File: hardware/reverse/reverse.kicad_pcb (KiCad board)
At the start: 2 copper layers, 40 x 40 mm, 41 parts, among them J1 Conn_01x04, J2 Conn_01x03, T1 TestPoint_THTPad_3.0x3.0mm_Dr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, T51 TestPoint_THTPad_D2.0mm_Drill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, T52 TestPoint_THTPad_D2.0mm_Drill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, T53 TestPoint_THTPad_D2.0mm_Drill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, T54 TestPoint_THTPad_D2.0mm_Drill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, T55 TestPoint_THTPad_D2.0mm_Drill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, T56 TestPoint_THTPad_D2.0mm_Drill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, U1 WCH CH32V003F4U6

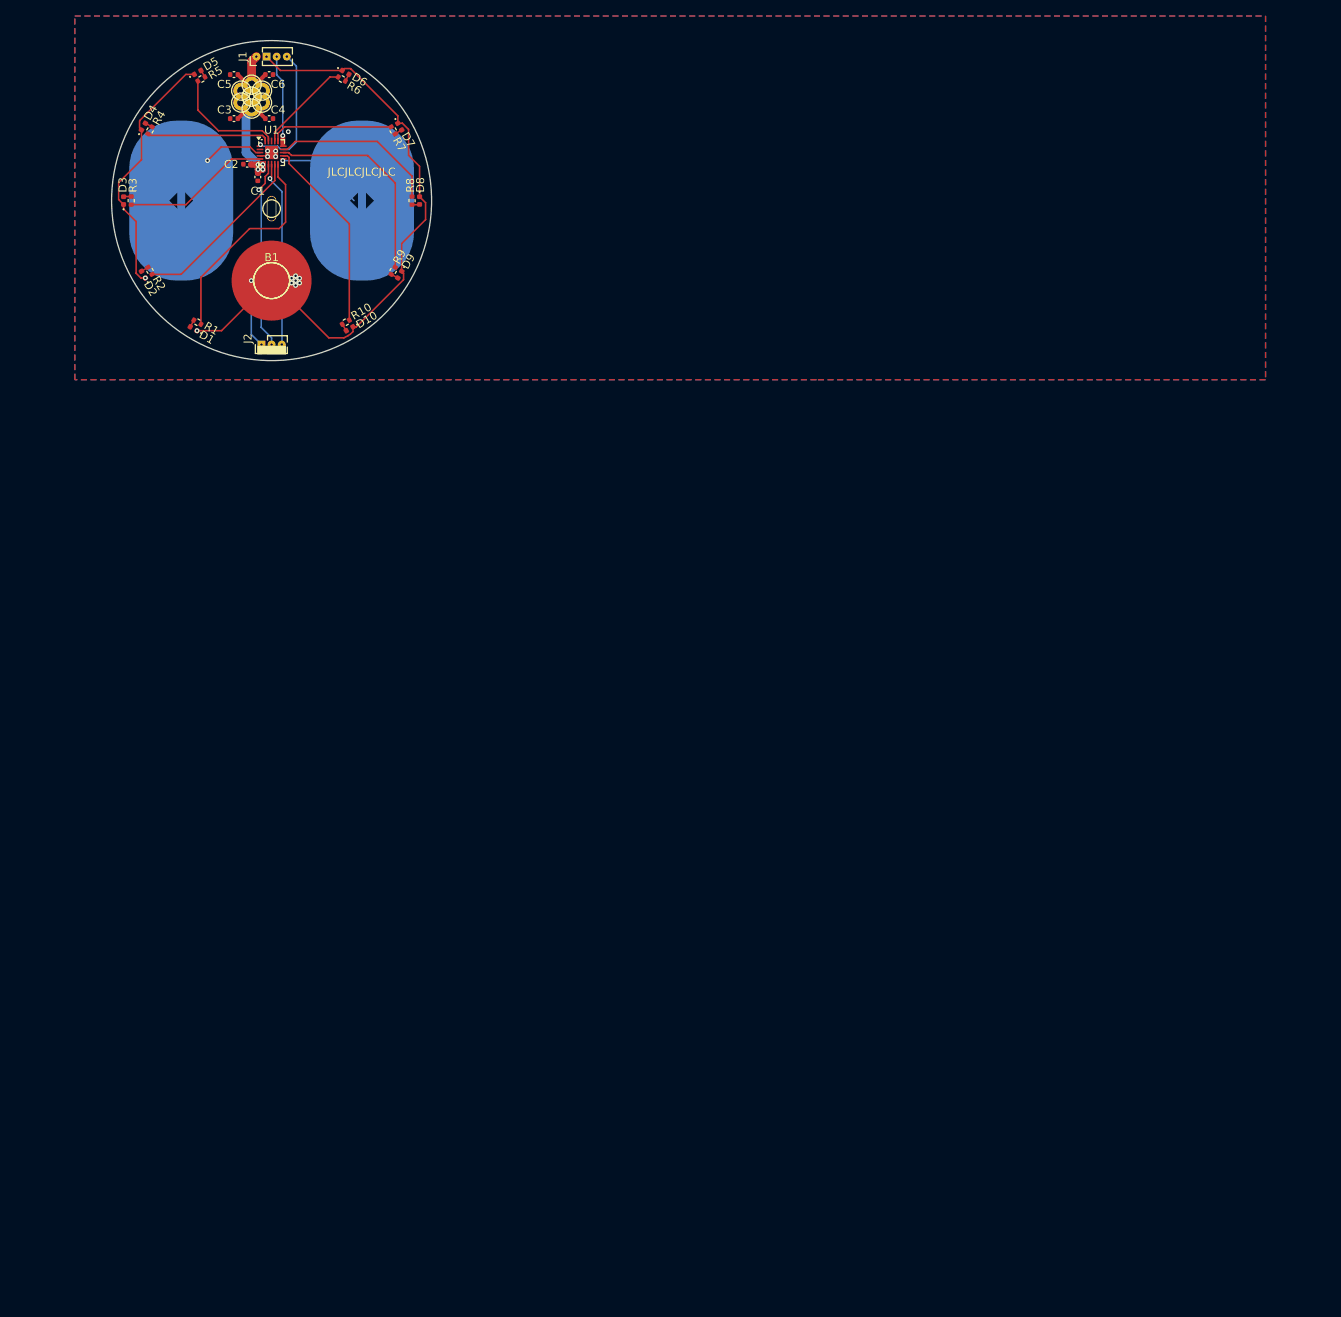
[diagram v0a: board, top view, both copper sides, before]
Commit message: separate boards and generate fab files
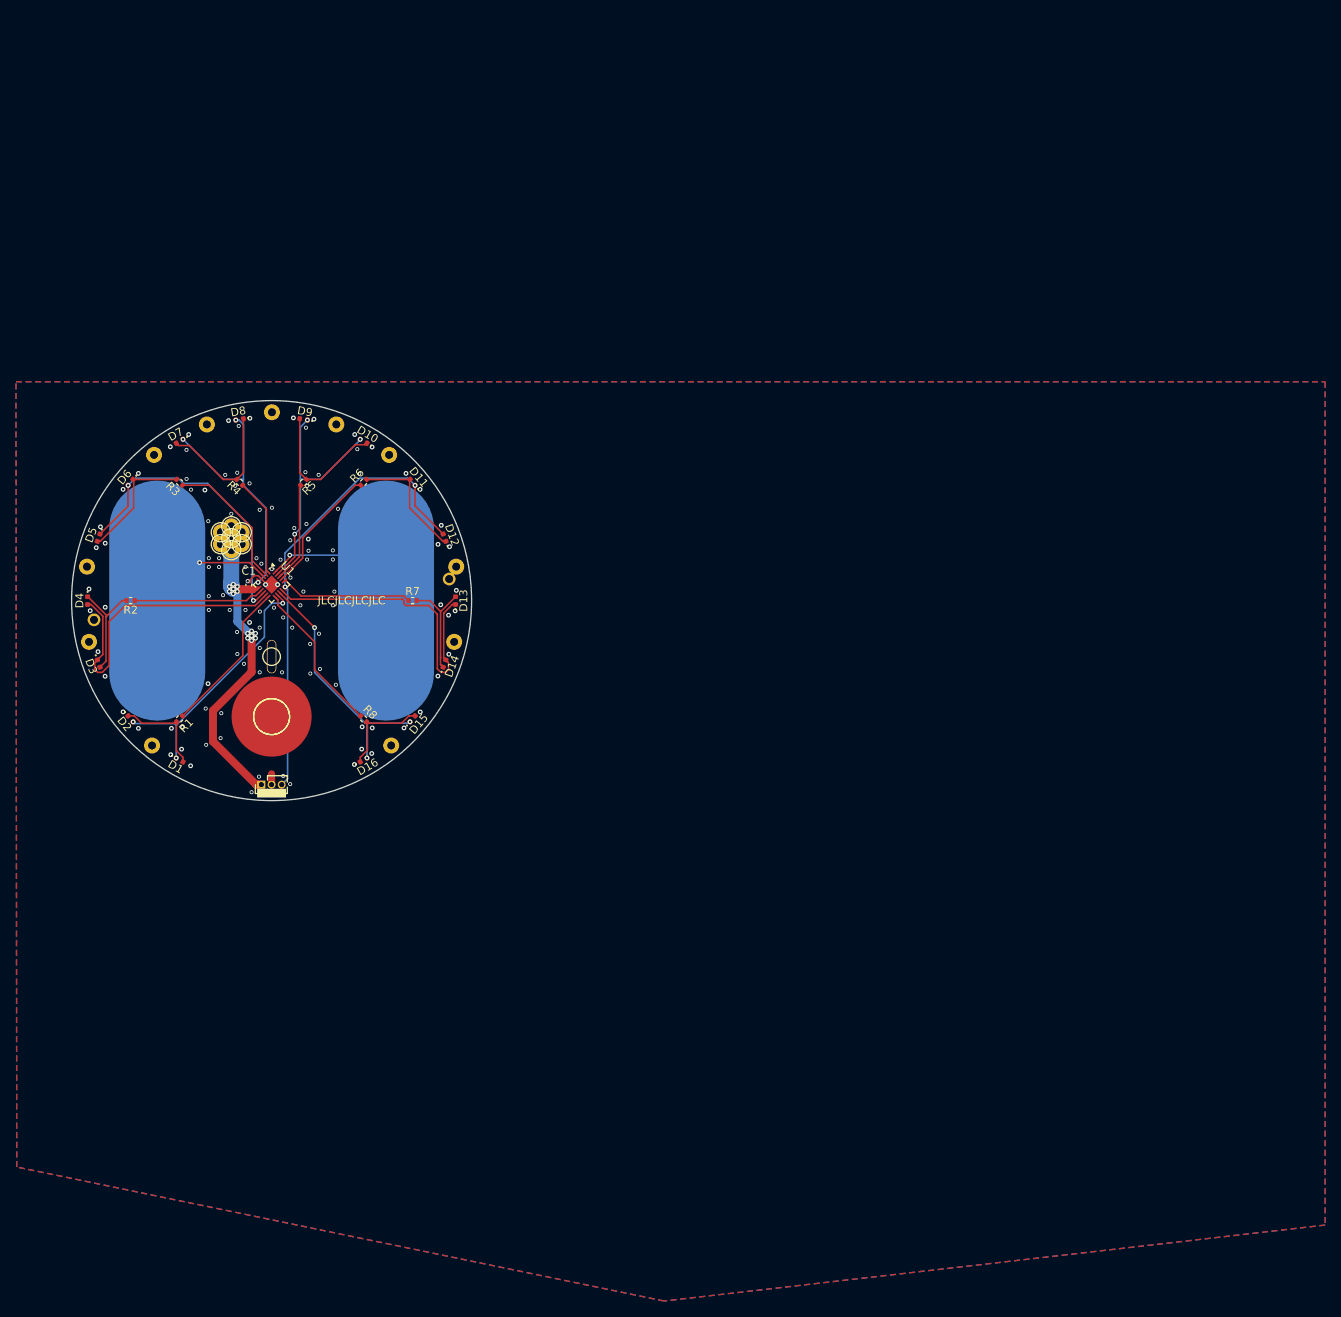
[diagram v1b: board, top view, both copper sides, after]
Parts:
- removed C2, C3, C4, C5, C6: 10n, Capacitor_SMD:C_0402_1005Metric
- removed J2: Conn_01x03, Connector_PinHeader_1.27mm:PinHeader_1x03_P1.27mm_Vertical
- removed R10, R9: 47R, Resistor_SMD:R_0402_1005Metric
- added D11: LED, LED_SMD:LED_0402_1005Metric, F.Cu at (67.6, 85.2)
- added D12: LED, LED_SMD:LED_0402_1005Metric, F.Cu at (71.6, 92.1)
- added D13: LED, LED_SMD:LED_0402_1005Metric, F.Cu at (73.0, 100.0)
- added D14: LED, LED_SMD:LED_0402_1005Metric, F.Cu at (71.6, 107.9)
- added D15: LED, LED_SMD:LED_0402_1005Metric, F.Cu at (67.6, 114.8)
- added D16: LED, LED_SMD:LED_0402_1005Metric, F.Cu at (61.5, 119.9)
- added align-r1: , , F.Cu at (27.8, 102.4)
- added align-r2: , , F.Cu at (72.2, 97.3)
- added stitch1: , , F.Cu at (26.9, 95.8)
- added stitch1: , , F.Cu at (58.1, 78.0)
- added stitch1: , , F.Cu at (50.0, 76.5)
- added stitch1: , , F.Cu at (41.9, 78.0)
- added stitch1: , , F.Cu at (27.2, 105.2)
- added stitch1: , , F.Cu at (35.3, 81.8)
- added stitch1: , , F.Cu at (35.1, 118.1)
- added stitch1: , , F.Cu at (64.9, 118.1)
- added stitch1: , , F.Cu at (73.1, 95.8)
- added stitch1: , , F.Cu at (64.7, 81.8)
- added stitch1: , , F.Cu at (72.8, 105.2)
- C1: value 10n -> 1u
- J1: value Conn_01x04 -> Conn_01x03; footprint Connector_PinHeader_1.27mm:PinHeader_1x04_P1.27mm_Vertical -> Connector_PinHeader_1.27mm:PinHeader_1x03_P1.27mm_Vertical
- moved J1 91.0 mm to (48.7, 123.0)
- moved R8 65.1 mm to (61.5, 114.8), turned to -45 degrees
- moved D4 59.7 mm to (27.0, 100.0), turned to -90 degrees
- moved D5 59.5 mm to (28.4, 92.1), turned to -110 degrees
- moved R7 58.8 mm to (67.6, 100.0), turned to 0 degrees
- moved D3 58.0 mm to (28.4, 107.9), turned to -70 degrees
- moved D6 57.9 mm to (32.4, 85.2), turned to -130 degrees
- moved battery-eject1 56.0 mm to (50.0, 107.0)
- moved D2 55.6 mm to (32.4, 114.8), turned to -50 degrees
- moved through-r1 55.3 mm to (45.0, 92.2)
- moved through-r2 55.3 mm to (45.0, 90.7)
- moved through-r3 55.3 mm to (46.3, 91.5)
- moved through-r4 55.3 mm to (46.3, 93.0)
- moved through-r5 55.3 mm to (45.0, 93.7)
- moved through-r6 55.3 mm to (43.7, 93.0)
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- renumbered S2 to S1, S1 to S2, T1 to battery-eject1, T51 to through-r1, T51 to through-r2, T52 to through-r3, T53 to through-r4, T54 to through-r5, T55 to through-r6, T56 to through-r7
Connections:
- net /LED1 renamed PWM1
- net /LED6 renamed PWM6
- net /LED7 renamed PWM7
- net /SWIO renamed GP6
- D1 pad 1: GND -> GP1
- D10 pad 1: GND -> Net-(D10-K)
- D10 pad 2: Net-(D10-A) -> GP5
- D2 pad 1: GND -> Net-(D1-A)
- D2 pad 2: Net-(D2-A) -> GP1
- D3 pad 1: GND -> GP2
- D4 pad 1: GND -> Net-(D3-A)
- D4 pad 2: Net-(D4-A) -> GP2
- D5 pad 1: GND -> GP3
- D6 pad 1: GND -> Net-(D5-A)
- D6 pad 2: Net-(D6-A) -> GP3
- D7 pad 1: GND -> GP4
- D8 pad 1: GND -> Net-(D7-A)
- D8 pad 2: Net-(D8-A) -> GP4
- D9 pad 1: GND -> GP5
- D9 pad 2: Net-(D9-A) -> Net-(D10-K)
- R2 pad 1: /LED2 -> PWM2
- R2 pad 2: Net-(D2-A) -> Net-(D3-A)
- R3 pad 1: /LED3 -> PWM3
- R3 pad 2: Net-(D3-A) -> Net-(D5-A)
- R4 pad 1: /LED4 -> PWM4
- R4 pad 2: Net-(D4-A) -> Net-(D7-A)
- R5 pad 1: /LED5 -> PWM5
- R5 pad 2: Net-(D5-A) -> Net-(D10-K)
- R6 pad 2: Net-(D6-A) -> Net-(D11-A)
- R7 pad 2: Net-(D7-A) -> Net-(D13-A)
- R8 pad 1: /LED8 -> PWM8
- R8 pad 2: Net-(D8-A) -> Net-(D15-A)
- S1 pad 1: /touch2 -> /touch1
- S2 pad 1: /touch1 -> /touch2
- U1 pad 1: /NRST -> PWM4
- U1 pad 11: /touch2 -> PWM8
- U1 pad 12: /LED10 -> GP1
- U1 pad 13: /LED9 -> GP8
- U1 pad 14: /LED8 -> GP7
- U1 pad 18: unconnected-(U1-PD4-Pad18) -> PWM5
- U1 pad 19: /LED5 -> GP5
- U1 pad 2: unconnected-(U1-PA1-Pad2) -> PWM3
- U1 pad 20: /LED4 -> /touch1
- U1 pad 3: /touch1 -> /touch2
- U1 pad 5: /LED3 -> GP4
- U1 pad 7: /TX -> PWM2
- U1 pad 8: /RX -> GP3
- U1 pad 9: /LED2 -> GP2
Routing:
- net GND: track 120.2 -> 4.28 mm, vias 15 -> 119
- net GP6: track 11.3 -> 57.6 mm, vias 1 -> 2
- net GP7: track 0.00 -> 38.6 mm
- net GP2: track 0.00 -> 38.3 mm
- net GP3: track 0.00 -> 37.0 mm, vias 0 -> 2
- net GP1: track 0.00 -> 32.5 mm, vias 0 -> 3
- net GP4: track 0.00 -> 32.4 mm, vias 0 -> 3
- net GP8: track 0.00 -> 30.8 mm, vias 0 -> 3
- net GP5: track 0.00 -> 30.5 mm, vias 0 -> 3
- net /LED9: track 26.1 -> 0.00 mm
- net /LED10: track 24.3 -> 0.00 mm
- net /TX: track 23.7 -> 0.00 mm, vias 1 -> 0
- net /RX: track 23.3 -> 0.00 mm, vias 1 -> 0
- net /LED2: track 22.2 -> 0.00 mm
- net /LED8: track 20.9 -> 0.00 mm
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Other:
- board size 40 x 40 mm -> 50 x 50 mm
- board text added: "3V"
- board text added: "SWD"
- board text added: "import QR SVG scale 0.2"

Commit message: separate into fab-able parts
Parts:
- moved D10 50.0 mm to (61.5, 30.1)
- moved D12 50.0 mm to (71.6, 42.1)
- moved D5 50.0 mm to (28.4, 42.1)
- moved D7 50.0 mm to (38.5, 30.1)
- moved D8 50.0 mm to (46.0, 27.3)
- moved D9 50.0 mm to (54.0, 27.3)
- moved align-r1 50.0 mm to (27.8, 52.4)
- moved stitch1 50.0 mm to (27.2, 55.2)
- moved stitch1 50.0 mm to (72.8, 55.2)
- moved - 50.0 mm to (50.0, 64.5)
- moved B1 50.0 mm to (50.0, 64.5)
- moved C1 50.0 mm to (47.1, 48.0)
- moved D1 50.0 mm to (38.5, 69.9)
- moved D11 50.0 mm to (67.6, 35.2)
- moved D13 50.0 mm to (73.0, 50.0)
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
